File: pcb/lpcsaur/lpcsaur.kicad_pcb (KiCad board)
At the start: 4 copper layers, 100 x 100 mm, 157 parts, among them IC1 74LV11, IC2 74LV10, IC3 74HCT08, IC4 74LVC07, IC5 74LVC07, IC6 LM1117-3.3, IC7 LPC1768_TQFP100, J1 X1, J10 LASER, J11 Motor X, J12 Motor Y, J13 Motor Z, J14 Motor AUX, J15 SSR, J16 SSR AUX, J17 RELAY1, J18 V-SELECT, J19 RELAY2, J2 X2, J20 V-SELECT, J21 USB_B, J22 RGB LED, J23 SERIAL, J24 5V IN, J25 12V IN, J26 24V IN, J27 AUX I/O, J28 CHILLER, J29 MICRO-SD, J3 Y1, J4 Y2, J5 Z1, J6 Z2, J7 DOOR1, J8 DOOR2, J9 E-STOP, Q1 ZXMN4A06, Q2 ZXMN4A06, Q3 BSL207SP, Q4 BSL207SP, SW1 SW_PUSH, SW2 SW_PUSH, SW3 SW_PUSH, X1 12 MHz

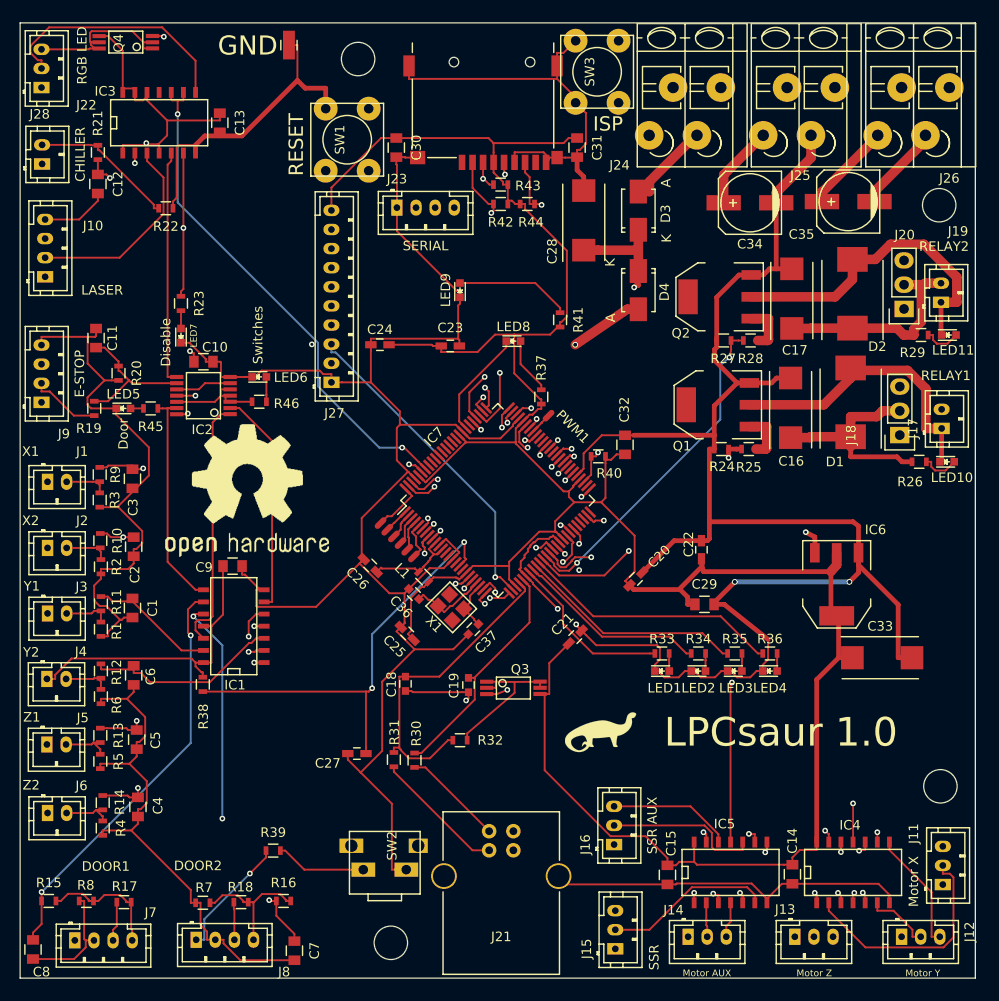
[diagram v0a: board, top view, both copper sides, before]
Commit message: Fix footprint for Q3, Q4.
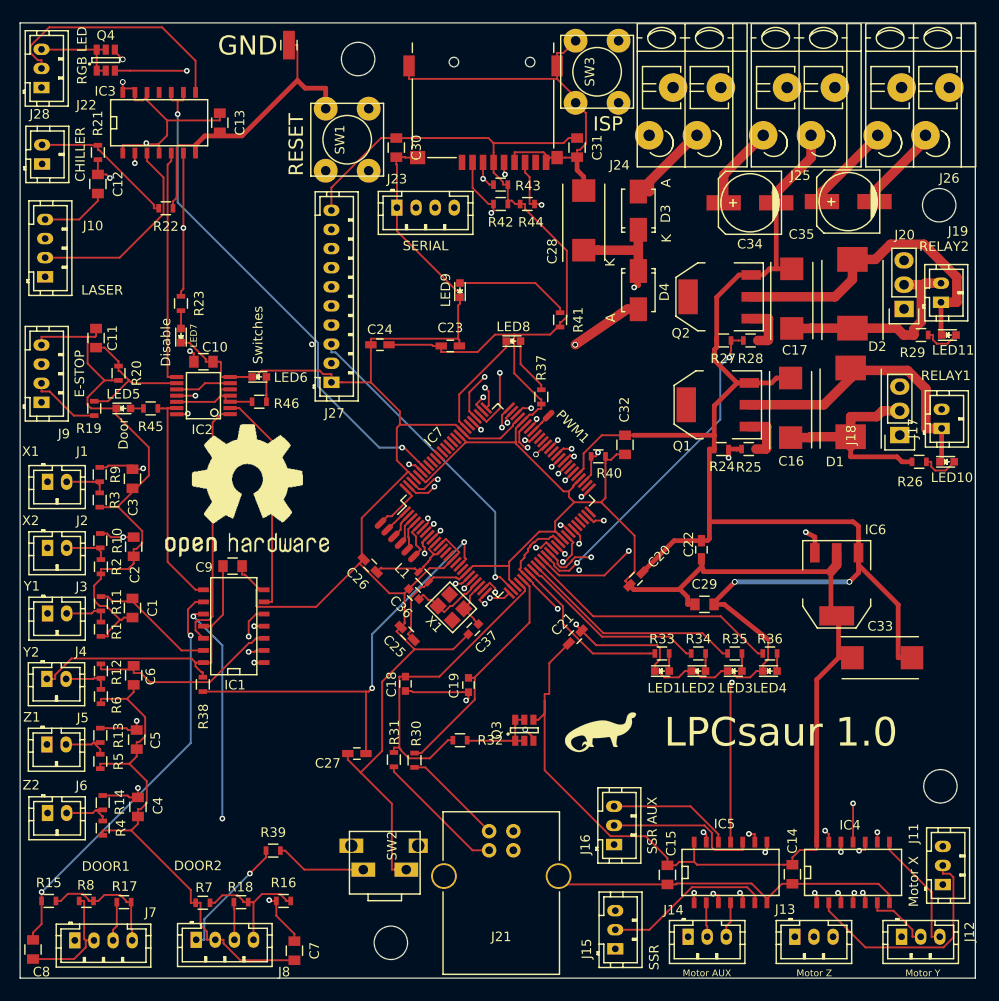
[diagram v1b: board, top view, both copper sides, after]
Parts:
- Q3, Q4: footprint lpcsaur:SSOP-6-3 -> TO_SOT_Packages_SMD:TSOP-6-DGS
- moved Q4 3.79 mm to (109.0, 53.9)
- moved Q3 3.35 mm to (152.8, 124.1), turned to 90 degrees
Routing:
- net Net-(J22-Pad3): track 17.5 -> 9.89 mm
- net Net-(Q3-PadD): track 16.2 -> 9.16 mm
- net P2.9: track 29.6 -> 32.3 mm
- net +3V3: track 460.2 -> 462.5 mm
- net P1.0: track 59.1 -> 61.3 mm
- net +5V: track 280.0 -> 278.3 mm, vias 1 -> 3

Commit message: Fix minor silkscreen issues.
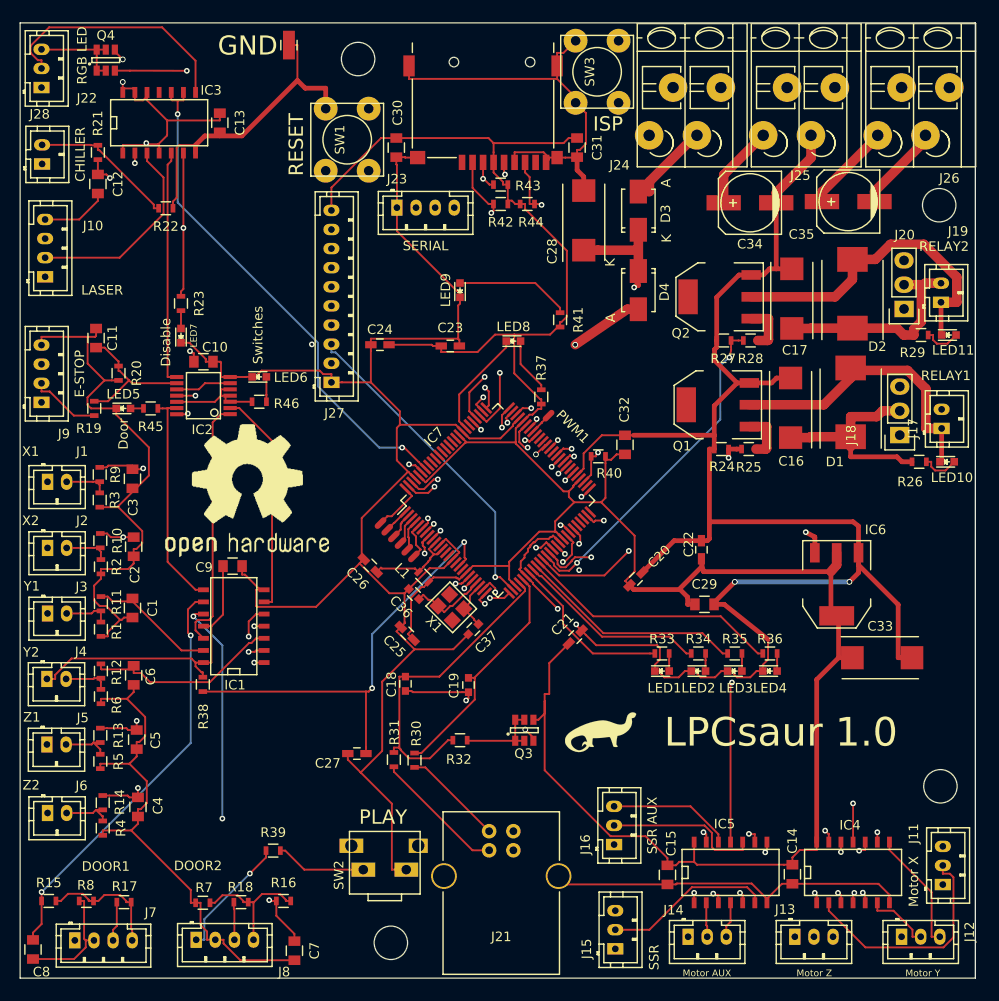
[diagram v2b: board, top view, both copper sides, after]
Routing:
- added copper zone on In2.Cu, net GND
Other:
- board text added: "PLAY"
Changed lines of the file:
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@@
     (links 367)
     (no_connects 0)
-    (area 99.949999 49.949999 200.050001 150.050001)
+    (area 99.709999 44.476999 218.044072 151.879)
     (thickness 1.6)
-    (drawings 8)
+    (drawings 9)
     (tracks 1797)
     (zones 0)
@@
     (trace_clearance 0.16)
     (zone_clearance 0.508)
-    (zone_45_only no)
+    (zone_45_only yes)
     (trace_min 0.16)
     (segment_width 0.2)
@@
     (pad_to_mask_clearance 0)
     (aux_axis_origin 0 0)
-    (visible_elements FFFFEF7F)
+    (visible_elements FFFFFF7F)
     (pcbplotparams
-      (layerselection 0x210f0_80000007)
+      (layerselection 0x210f8_80000007)
       (usegerberextensions true)
       (excludeedgelayer true)
@@
       (drillshape 0)
       (scaleselection 1)
-      (outputdirectory gerber/protel/))
+      (outputdirectory gerber/))
   )
   (net 0 "")
@@
   (module lpcsaur2:TactileSwitchUpright (layer F.Cu)
     (at 138.176 136.144 270)
-    (fp_text reference SW2 (at 0 -0.762 270) (layer F.SilkS)
+    (fp_text reference SW2 (at 3.0734 4.8006 270) (layer F.SilkS)
       (effects (font (size 1 1) (thickness 0.15)))
     )
@@
     (tags "resistor 0603")
     (attr smd)
-    (fp_text reference R32 (at -3.175 0 180) (layer F.SilkS)
+    (fp_text reference R32 (at 0.127 -2.0066 180) (layer F.SilkS)
       (effects (font (size 1 1) (thickness 0.15)))
     )
@@
     (tags "capacitor 0805")
     (attr smd)
-    (fp_text reference C30 (at 0 -2.1 270) (layer F.SilkS)
+    (fp_text reference C30 (at -3.6449 -0.1402 270) (layer F.SilkS)
       (effects (font (size 1 1) (thickness 0.15)))
     )
@@
     (tags "CMS SOJ")
     (attr smd)
-    (fp_text reference IC3 (at -5.6515 -3.175) (layer F.SilkS)
+    (fp_text reference IC3 (at 5.4356 -3.2766) (layer F.SilkS)
       (effects (font (size 1 1) (thickness 0.15)))
     )
@@
     (descr http://www.jst-mfg.com/product/pdf/eng/ePH.pdf)
     (tags "connector jst ph")
-    (fp_text reference J22 (at -1.8415 4.699 180) (layer F.SilkS)
+    (fp_text reference J22 (at -1.1176 4.7498 180) (layer F.SilkS)
       (effects (font (size 1 1) (thickness 0.15)))
     )
@@
     (tags SOT-23-6)
     (attr smd)
-    (fp_text reference Q3 (at 0 -2.9 90) (layer F.SilkS)
+    (fp_text reference Q3 (at -2.4384 -0.0762 180) (layer F.SilkS)
       (effects (font (size 1 1) (thickness 0.15)))
     )
@@
     )
   )
+  (gr_text PLAY (at 137.9982 133.1468) (layer F.SilkS)
+    (effects (font (size 1.5 1.5) (thickness 0.3)))
+  )
   (gr_text ISP (at 161.544 60.579) (layer F.SilkS)
     (effects (font (size 1.5 1.5) (thickness 0.3)))
@@
   (segment (start 151.831 123.6836) (end 151.831 125.1536) (width 0.2) (layer F.Cu) (net 123))
   (segment (start 152.781 122.9536) (end 151.831 122.9536) (width 0.2) (layer F.Cu) (net 123))
+  (zone (net 2) (net_name GND) (layer In2.Cu) (hatch edge 0.508)
+    (connect_pads (clearance 0.508))
+    (min_thickness 0.254)
+    (fill yes (arc_segments 16) (thermal_gap 0.508) (thermal_bridge_width 0.508))
+    (polygon
+      (pts
+        (xy 100.3808 50.1142) (xy 199.4916 50.1142) (xy 199.4916 149.5298) (xy 100.2284 149.5298) (xy 100.2284 50.2666)
+        (xy 100.5332 50.2666)
+      )
+    )
+  )
 )
